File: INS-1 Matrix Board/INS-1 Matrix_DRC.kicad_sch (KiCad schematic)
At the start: 134 parts, among them J1 Conn_02x04_Odd_Even, J2 Conn_02x04_Odd_Even, T0 INS-1, T1 INS-1, T10 INS-1, T11 INS-1, T12 INS-1, T13 INS-1, T14 INS-1, T15 INS-1, T16 INS-1, T17 INS-1, T18 INS-1, T19 INS-1, T2 INS-1, T20 INS-1, T21 INS-1, T22 INS-1, T23 INS-1, T24 INS-1, T25 INS-1, T26 INS-1, T27 INS-1, T28 INS-1, T29 INS-1, T3 INS-1, T30 INS-1, T31 INS-1, T32 INS-1, T33 INS-1, T34 INS-1, T35 INS-1, T36 INS-1, T37 INS-1, T38 INS-1, T39 INS-1, T4 INS-1, T40 INS-1, T41 INS-1, T42 INS-1, T43 INS-1, T44 INS-1, T45 INS-1, T46 INS-1, T47 INS-1, T48 INS-1, T49 INS-1, T5 INS-1, T50 INS-1, T51 INS-1, T52 INS-1, T53 INS-1, T54 INS-1, T55 INS-1, T56 INS-1, T57 INS-1, T58 INS-1, T59 INS-1, T6 INS-1, T7 INS-1, T8 INS-1, T9 INS-1, U1 HV5530, U2 HV5530

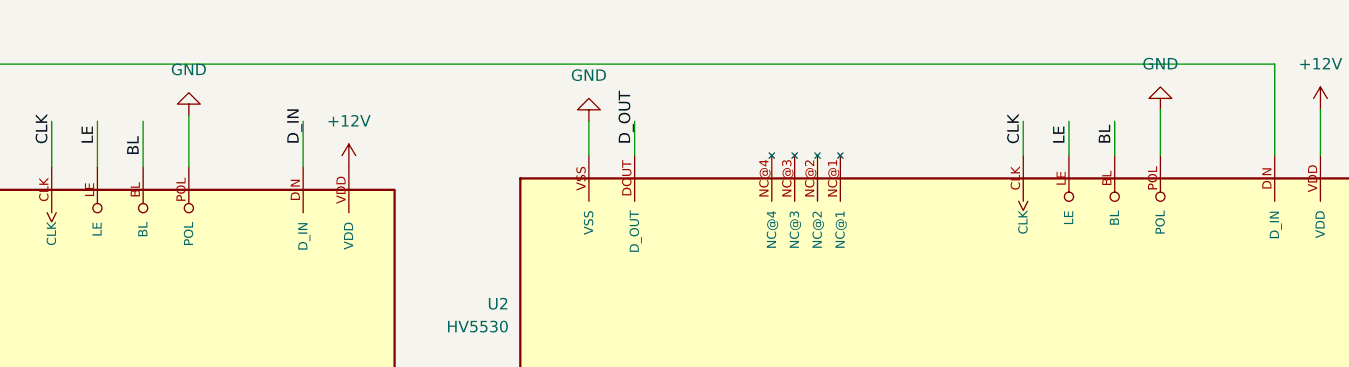
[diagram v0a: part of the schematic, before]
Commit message: Change POL pin to connect to 12V
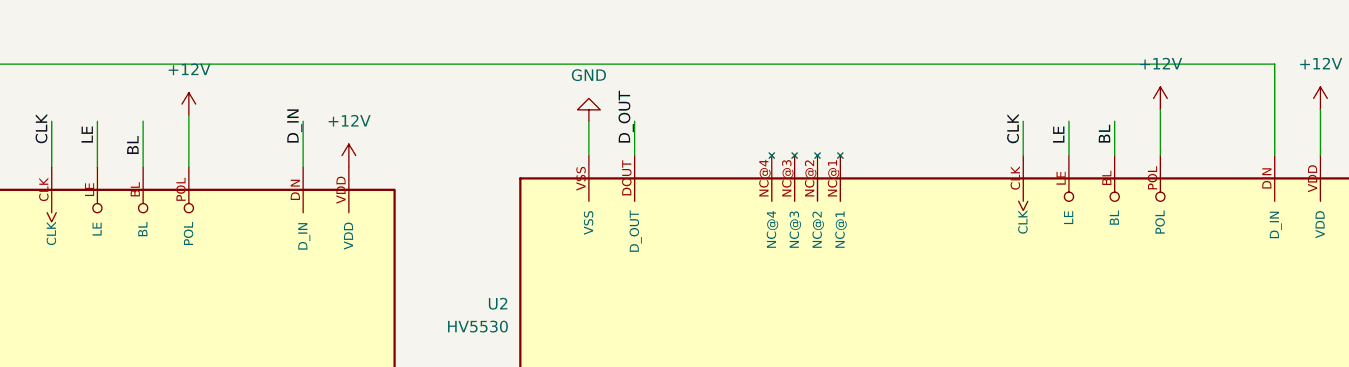
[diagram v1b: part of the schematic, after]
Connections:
- net +12V: now also U1.POL, U2.POL
- net GND: no longer U1.POL, U2.POL
